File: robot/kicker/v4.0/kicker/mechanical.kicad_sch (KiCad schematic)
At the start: 12 parts

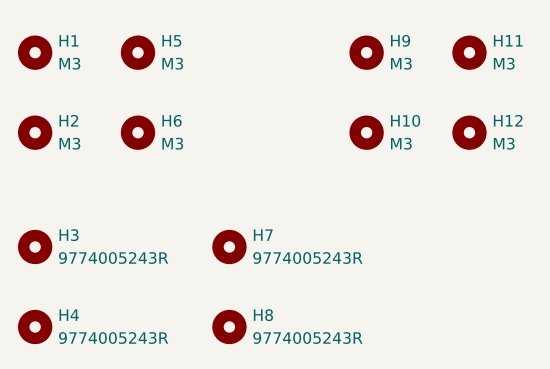
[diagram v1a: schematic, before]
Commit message: initial board structure from dxf
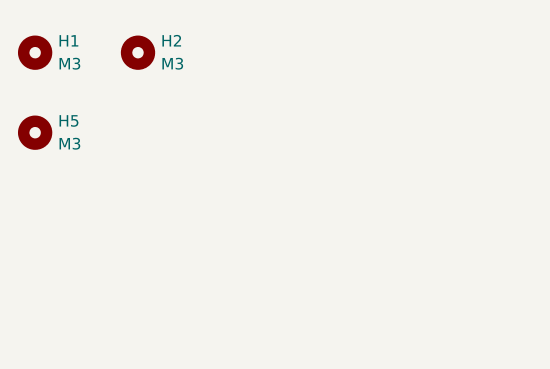
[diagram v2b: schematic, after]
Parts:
- removed H10, H11, H12, H6, H9: M3, MountingHole:MountingHole_3.2mm_M3_Pad, symbol Mechanical:MountingHole
- removed H3, H4, H7, H8: 9774005243R, AT-Mechanical:WE-9774005243R, symbol Mechanical:MountingHole
- renumbered H5 to H2, H2 to H5

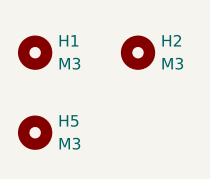
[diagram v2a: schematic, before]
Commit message: Adjust for mechanical constraints and route board
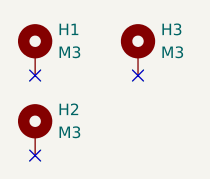
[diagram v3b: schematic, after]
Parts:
- H1: symbol Mechanical:MountingHole -> Mechanical:MountingHole_Pad
- H2: renamed from H5; symbol Mechanical:MountingHole -> Mechanical:MountingHole_Pad
- H3: renamed from H2; symbol Mechanical:MountingHole -> Mechanical:MountingHole_Pad
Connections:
- no-connect marks 0 -> 3
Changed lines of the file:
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@@
 		(comment 1 "W. Stuckey")
 	)
+	(no_connect
+		(at 25.4 36.83)
+	)
+	(no_connect
+		(at 36.83 27.94)
+	)
+	(no_connect
+		(at 25.4 27.94)
+	)
 	(symbol
-		(lib_id "Mechanical:MountingHole")
+		(lib_id "Mechanical:MountingHole_Pad")
 		(at 36.83 25.4 0)
 		(unit 1)
-		(exclude_from_sim no)
+		(exclude_from_sim yes)
+		(in_bom no)
+		(on_board yes)
+		(dnp no)
+		(fields_autoplaced yes)
+		(property "Reference" "H3"
+			(at 39.37 22.8599 0)
+			(effects
+				(font
+					(size 1.27 1.27)
+				)
+				(justify left)
+			)
+		)
+		(property "Value" "M3"
+			(at 39.37 25.3999 0)
+			(effects
+				(font
+					(size 1.27 1.27)
+				)
+				(justify left)
+			)
+		)
+		(property "Footprint" "MountingHole:MountingHole_3.2mm_M3_Pad"
+			(at 36.83 25.4 0)
+			(effects
+				(font
+					(size 1.27 1.27)
+				)
+				(hide yes)
+			)
+		)
+		(property "Datasheet" "~"
+			(at 36.83 25.4 0)
+			(effects
+				(font
+					(size 1.27 1.27)
+				)
+				(hide yes)
+			)
+		)
+		(property "Description" "Mounting Hole with connection"
+			(at 36.83 25.4 0)
+			(effects
+				(font
+					(size 1.27 1.27)
+				)
+				(hide yes)
+			)
+		)
+		(pin "1"
+		)
+		(instances
+			(project "kicker"
+				(path "/7c007fad-bfbf-4e78-a837-1f8089552516/4d5d86cd-ec95-402a-873b-72ed338f41dd"
+					(reference "H3")
+					(unit 1)
+				)
+			)
+		)
+	)
+	(symbol
+		(lib_id "Mechanical:MountingHole_Pad")
+		(at 25.4 25.4 0)
+		(unit 1)
+		(exclude_from_sim yes)
+		(in_bom no)
+		(on_board yes)
+		(dnp no)
+		(fields_autoplaced yes)
+		(property "Reference" "H1"
+			(at 27.94 22.8599 0)
+			(effects
+				(font
+					(size 1.27 1.27)
+				)
+				(justify left)
+			)
+		)
+		(property "Value" "M3"
+			(at 27.94 25.3999 0)
+			(effects
+				(font
+					(size 1.27 1.27)
+				)
+				(justify left)
+			)
+		)
+		(property "Footprint" "MountingHole:MountingHole_3.2mm_M3_Pad"
+			(at 25.4 25.4 0)
+			(effects
+				(font
+					(size 1.27 1.27)
+				)
+				(hide yes)
+			)
+		)
+		(property "Datasheet" "~"
+			(at 25.4 25.4 0)
+			(effects
+				(font
+					(size 1.27 1.27)
+				)
+				(hide yes)
+			)
+		)
+		(property "Description" "Mounting Hole with connection"
+			(at 25.4 25.4 0)
+			(effects
+				(font
+					(size 1.27 1.27)
+				)
+				(hide yes)
+			)
+		)
+		(pin "1"
+		)
+		(instances
+			(project "kicker"
+				(path "/7c007fad-bfbf-4e78-a837-1f8089552516/4d5d86cd-ec95-402a-873b-72ed338f41dd"
+					(reference "H1")
+					(unit 1)
+				)
+			)
+		)
+	)
+	(symbol
+		(lib_id "Mechanical:MountingHole_Pad")
+		(at 25.4 34.29 0)
+		(unit 1)
+		(exclude_from_sim yes)
 		(in_bom no)
 		(on_board yes)
@@
 		(fields_autoplaced yes)
 		(property "Reference" "H2"
-			(at 39.37 24.13 0)
+			(at 27.94 31.7499 0)
 			(effects
 				(font
@@
 		)
 		(property "Value" "M3"
-			(at 39.37 26.67 0)
+			(at 27.94 34.2899 0)
 			(effects
 				(font
@@
 		)
 		(property "Footprint" "MountingHole:MountingHole_3.2mm_M3_Pad"
-			(at 36.83 25.4 0)
+			(at 25.4 34.29 0)
 			(effects
 				(font
@@
 		)
 		(property "Datasheet" "~"
-			(at 36.83 25.4 0)
-			(effects
-				(font
-					(size 1.27 1.27)
-				)
-				(hide yes)
-			)
-		)
-		(property "Description" "Mounting Hole without connection"
-			(at 36.83 25.4 0)
-			(effects
-				(font
-					(size 1.27 1.27)
-				)
-				(hide yes)
-			)
+			(at 25.4 34.29 0)
+			(effects
+				(font
+					(size 1.27 1.27)
+				)
+				(hide yes)
+			)
+		)
+		(property "Description" "Mounting Hole with connection"
+			(at 25.4 34.29 0)
+			(effects
+				(font
+					(size 1.27 1.27)
+				)
+				(hide yes)
+			)
+		)
+		(pin "1"
 		)
 		(instances
@@
 					(unit 1)
 				)
-			)
-		)
-	)
-	(symbol
-		(lib_id "Mechanical:MountingHole")
-		(at 25.4 25.4 0)
-		(unit 1)
-		(exclude_from_sim no)
-		(in_bom no)
-		(on_board yes)
-		(dnp no)
-		(fields_autoplaced yes)
-		(property "Reference" "H1"
-			(at 27.94 24.13 0)
-			(effects
-				(font
-					(size 1.27 1.27)
-				)
-				(justify left)
-			)
-		)
-		(property "Value" "M3"
-			(at 27.94 26.67 0)
-			(effects
-				(font
-					(size 1.27 1.27)
-				)
-				(justify left)
-			)
-		)
-		(property "Footprint" "MountingHole:MountingHole_3.2mm_M3_Pad"
-			(at 25.4 25.4 0)
-			(effects
-				(font
-					(size 1.27 1.27)
-				)
-				(hide yes)
-			)
-		)
-		(property "Datasheet" "~"
-			(at 25.4 25.4 0)
-			(effects
-				(font
-					(size 1.27 1.27)
-				)
-				(hide yes)
-			)
-		)
-		(property "Description" "Mounting Hole without connection"
-			(at 25.4 25.4 0)
-			(effects
-				(font
-					(size 1.27 1.27)
-				)
-				(hide yes)
-			)
-		)
-		(instances
-			(project "kicker"
-				(path "/7c007fad-bfbf-4e78-a837-1f8089552516/4d5d86cd-ec95-402a-873b-72ed338f41dd"
-					(reference "H1")
-					(unit 1)
-				)
-			)
-		)
-	)
-	(symbol
-		(lib_id "Mechanical:MountingHole")
-		(at 25.4 34.29 0)
-		(unit 1)
-		(exclude_from_sim no)
-		(in_bom no)
-		(on_board yes)
-		(dnp no)
-		(fields_autoplaced yes)
-		(property "Reference" "H5"
-			(at 27.94 33.02 0)
-			(effects
-				(font
-					(size 1.27 1.27)
-				)
-				(justify left)
-			)
-		)
-		(property "Value" "M3"
-			(at 27.94 35.56 0)
-			(effects
-				(font
-					(size 1.27 1.27)
-				)
-				(justify left)
-			)
-		)
-		(property "Footprint" "MountingHole:MountingHole_3.2mm_M3_Pad"
-			(at 25.4 34.29 0)
-			(effects
-				(font
-					(size 1.27 1.27)
-				)
-				(hide yes)
-			)
-		)
-		(property "Datasheet" "~"
-			(at 25.4 34.29 0)
-			(effects
-				(font
-					(size 1.27 1.27)
-				)
-				(hide yes)
-			)
-		)
-		(property "Description" "Mounting Hole without connection"
-			(at 25.4 34.29 0)
-			(effects
-				(font
-					(size 1.27 1.27)
-				)
-				(hide yes)
-			)
-		)
-		(instances
-			(project "kicker"
-				(path "/7c007fad-bfbf-4e78-a837-1f8089552516/4d5d86cd-ec95-402a-873b-72ed338f41dd"
-					(reference "H5")
-					(unit 1)
-				)
